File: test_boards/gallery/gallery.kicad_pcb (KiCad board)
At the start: 2 copper layers, 22 parts

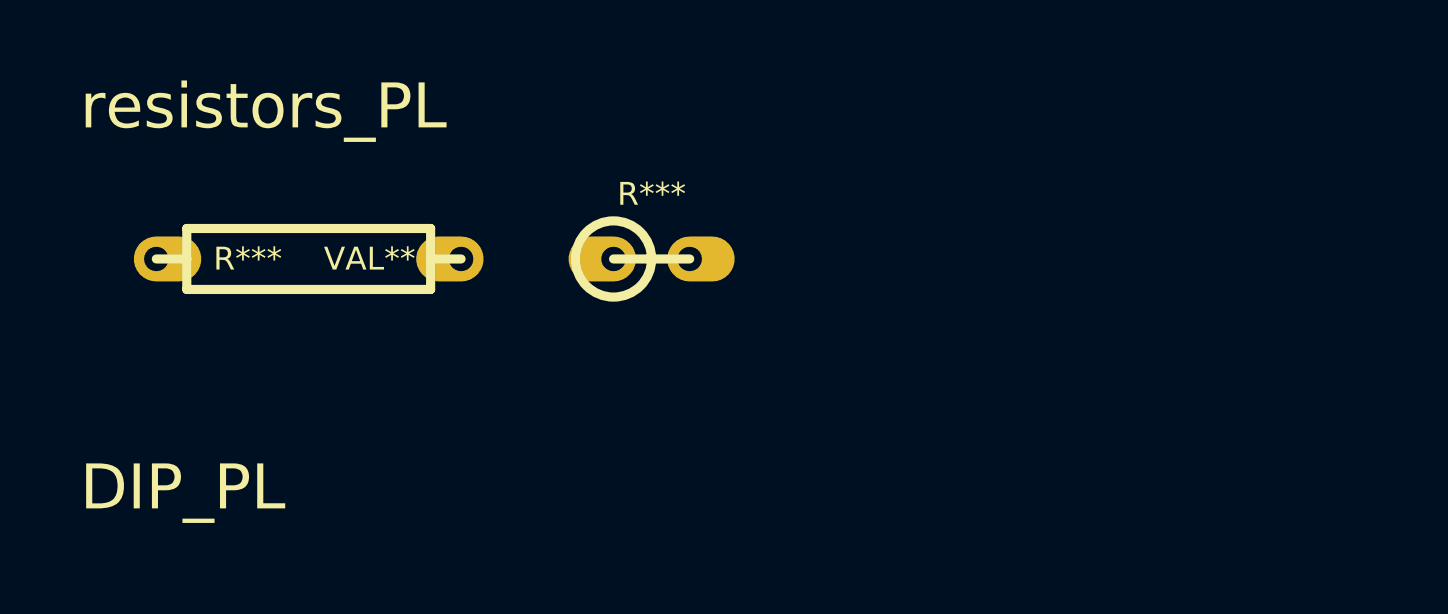
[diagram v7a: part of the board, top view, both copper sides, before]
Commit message: adding 1/2 watt resistor footprint
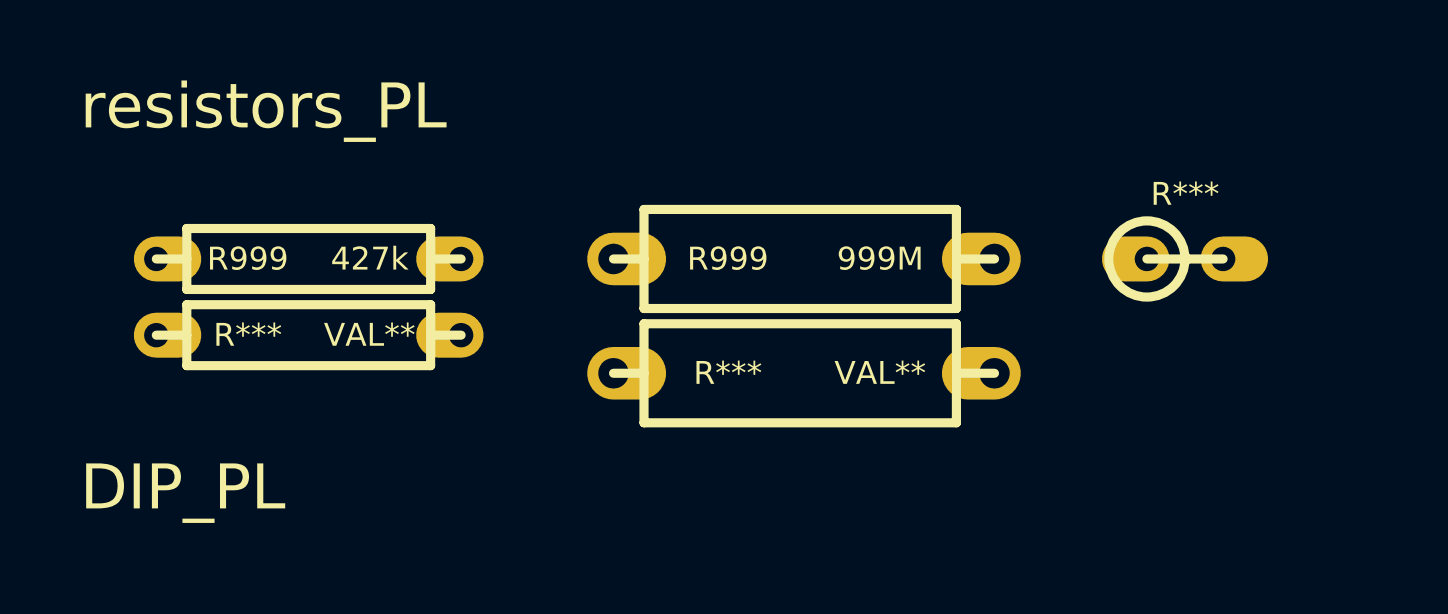
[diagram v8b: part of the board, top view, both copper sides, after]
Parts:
- added R***: VAL**, R_AXIAL_0W25, F.Cu at (20.3, 25.4)
- added R***: VAL**, R_AXIAL_0W5, F.Cu at (35.6, 26.7)
- added R999: 999M, R_AXIAL_0W5, F.Cu at (35.6, 22.9)
- R999: renamed from R***; value VAL** -> 427k
- moved R*** 17.8 mm to (53.3, 22.9)
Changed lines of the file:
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@@
     (tracks 22)
     (zones 0)
-    (modules 22)
+    (modules 25)
     (nets 1)
   )
@@
     (pcb_text_width 0.3)
     (pcb_text_size 1.5 1.5)
-    (mod_edge_width 0.15)
+    (mod_edge_width 0.3048)
     (mod_text_size 1 1)
     (mod_text_width 0.15)
-    (pad_size 9.144 9.144)
-    (pad_drill 6.096)
+    (pad_size 2.6289 1.7526)
+    (pad_drill 1.016)
     (pad_to_mask_clearance 0)
     (aux_axis_origin 0 0)
@@
     (tags R)
     (autoplace_cost180 10)
-    (fp_text reference R*** (at 3.048 0) (layer F.SilkS)
-      (effects (font (size 0.762 0.762) (thickness 0.1524)))
-    )
-    (fp_text value VAL** (at 7.112 0) (layer F.SilkS)
+    (fp_text reference R999 (at 3.048 0) (layer F.SilkS)
+      (effects (font (size 0.762 0.762) (thickness 0.1524)))
+    )
+    (fp_text value 427k (at 7.112 0) (layer F.SilkS)
       (effects (font (size 0.762 0.762) (thickness 0.1524)))
     )
@@
   )
   (module R_AXIAL_0W25_V (layer F.Cu)
-    (at 35.56 22.86)
+    (at 53.34 22.86)
     (descr "1/4W resistor, vertical")
     (tags R)
@@
     )
   )
+  (module R_AXIAL_0W25 (layer F.Cu)
+    (at 20.32 25.4)
+    (descr "Resistor Axial 1/4W 0.4\"")
+    (tags R)
+    (autoplace_cost180 10)
+    (fp_text reference R*** (at 3.048 0) (layer F.SilkS)
+      (effects (font (size 0.762 0.762) (thickness 0.1524)))
+    )
+    (fp_text value VAL** (at 7.112 0) (layer F.SilkS)
+      (effects (font (size 0.762 0.762) (thickness 0.1524)))
+    )
+    (fp_line (start 0 0) (end 1.016 0) (layer F.SilkS) (width 0.3048))
+    (fp_line (start 1.016 0) (end 1.016 -1.016) (layer F.SilkS) (width 0.3048))
+    (fp_line (start 1.016 -1.016) (end 9.144 -1.016) (layer F.SilkS) (width 0.3048))
+    (fp_line (start 9.144 -1.016) (end 9.144 1.016) (layer F.SilkS) (width 0.3048))
+    (fp_line (start 9.144 1.016) (end 1.016 1.016) (layer F.SilkS) (width 0.3048))
+    (fp_line (start 1.016 1.016) (end 1.016 0) (layer F.SilkS) (width 0.3048))
+    (fp_line (start 10.16 0) (end 9.144 0) (layer F.SilkS) (width 0.3048))
+    (pad 1 thru_hole oval (at 0 0) (size 2.2479 1.4986) (drill 0.8128 (offset 0.37465 0))
+      (layers *.Cu *.Mask F.SilkS)
+    )
+    (pad 2 thru_hole oval (at 10.16 0) (size 2.2479 1.4986) (drill 0.8128 (offset -0.37465 0))
+      (layers *.Cu *.Mask F.SilkS)
+    )
+    (model discret/resistor.wrl
+      (at (xyz 0 0 0))
+      (scale (xyz 0.4 0.4 0.4))
+      (rotate (xyz 0 0 0))
+    )
+  )
+  (module R_AXIAL_0W5 (layer F.Cu)
+    (at 35.56 22.86)
+    (descr "Resistor Axial 1/2W 0.5\"")
+    (tags R)
+    (autoplace_cost180 10)
+    (fp_text reference R999 (at 3.81 0) (layer F.SilkS)
+      (effects (font (size 0.762 0.762) (thickness 0.1524)))
+    )
+    (fp_text value 999M (at 8.89 0) (layer F.SilkS)
+      (effects (font (size 0.762 0.762) (thickness 0.1524)))
+    )
+    (fp_line (start 12.7 0) (end 11.43 0) (layer F.SilkS) (width 0.3048))
+    (fp_line (start 1.016 1.651) (end 11.43 1.651) (layer F.SilkS) (width 0.3048))
+    (fp_line (start 11.43 -1.651) (end 1.016 -1.651) (layer F.SilkS) (width 0.3048))
+    (fp_line (start 11.43 -1.651) (end 11.43 1.651) (layer F.SilkS) (width 0.3048))
+    (fp_line (start 1.016 0) (end 1.016 1.651) (layer F.SilkS) (width 0.3048))
+    (fp_line (start 1.016 0) (end 1.016 -1.651) (layer F.SilkS) (width 0.3048))
+    (fp_line (start 0 0) (end 1.016 0) (layer F.SilkS) (width 0.3048))
+    (pad 1 thru_hole oval (at 0 0) (size 2.6289 1.7526) (drill 1.016 (offset 0.43815 0))
+      (layers *.Cu *.Mask F.SilkS)
+    )
+    (pad 2 thru_hole oval (at 12.7 0) (size 2.6289 1.7526) (drill 1.016 (offset -0.43815 0))
+      (layers *.Cu *.Mask F.SilkS)
+    )
+    (model discret/resistor.wrl
+      (at (xyz 0 0 0))
+      (scale (xyz 0.4 0.4 0.4))
+      (rotate (xyz 0 0 0))
+    )
+  )
+  (module R_AXIAL_0W5 (layer F.Cu)
+    (at 35.56 26.67)
+    (descr "Resistor Axial 1/2W 0.5\"")
+    (tags R)
+    (autoplace_cost180 10)
+    (fp_text reference R*** (at 3.81 0) (layer F.SilkS)
+      (effects (font (size 0.762 0.762) (thickness 0.1524)))
+    )
+    (fp_text value VAL** (at 8.89 0) (layer F.SilkS)
+      (effects (font (size 0.762 0.762) (thickness 0.1524)))
+    )
+    (fp_line (start 12.7 0) (end 11.43 0) (layer F.SilkS) (width 0.3048))
+    (fp_line (start 1.016 1.651) (end 11.43 1.651) (layer F.SilkS) (width 0.3048))
+    (fp_line (start 11.43 -1.651) (end 1.016 -1.651) (layer F.SilkS) (width 0.3048))
+    (fp_line (start 11.43 -1.651) (end 11.43 1.651) (layer F.SilkS) (width 0.3048))
+    (fp_line (start 1.016 0) (end 1.016 1.651) (layer F.SilkS) (width 0.3048))
+    (fp_line (start 1.016 0) (end 1.016 -1.651) (layer F.SilkS) (width 0.3048))
+    (fp_line (start 0 0) (end 1.016 0) (layer F.SilkS) (width 0.3048))
+    (pad 1 thru_hole oval (at 0 0) (size 2.6289 1.7526) (drill 1.016 (offset 0.43815 0))
+      (layers *.Cu *.Mask F.SilkS)
+    )
+    (pad 2 thru_hole oval (at 12.7 0) (size 2.6289 1.7526) (drill 1.016 (offset -0.43815 0))
+      (layers *.Cu *.Mask F.SilkS)
+    )
+    (model discret/resistor.wrl
+      (at (xyz 0 0 0))
+      (scale (xyz 0.4 0.4 0.4))
+      (rotate (xyz 0 0 0))
+    )
+  )
